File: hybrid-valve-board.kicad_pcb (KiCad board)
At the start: 2 copper layers, 68 x 79 mm, 45 parts, among them J1 XV Supply, J10 ARM, J2 MCU Supply, J3 XV In, J4 XV In, J5 XV In, J6 Continuity, J7 XV Out, J8 XV Out, J9 XV Out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

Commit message: Move arming LED closer to arming switch
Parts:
- moved D10 6.06 mm to (133.0, 84.0), turned to 0 degrees
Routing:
- net +3V3: track 33.4 -> 27.2 mm
- net Net-(D10-K): track 2.51 -> 7.66 mm
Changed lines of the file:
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@@
 		(tags "SMD DIP DIL PDIP SMDIP 2.54mm 9.53mm 375mil")
 		(property "Reference" "U2"
-			(at 0 -3.6 0)
+			(at 0 0 0)
 			(layer "F.SilkS")
 			(effects
@@
 		(tags "SMD DIP DIL PDIP SMDIP 2.54mm 9.53mm 375mil")
 		(property "Reference" "U3"
-			(at 0 -3.6 0)
+			(at 0 0 0)
 			(layer "F.SilkS")
 			(effects
@@
 		(tags "SMD DIP DIL PDIP SMDIP 2.54mm 9.53mm 375mil")
 		(property "Reference" "U4"
-			(at 0 -3.6 0)
+			(at 0 0 0)
 			(layer "F.SilkS")
 			(effects
@@
 	(footprint "LED_SMD:LED_0805_2012Metric_Pad1.15x1.40mm_HandSolder"
 		(layer "F.Cu")
-		(at 127.5 86.5 -90)
+		(at 133.025 84)
 		(descr "LED SMD 0805 (2012 Metric), square (rectangular) end terminal, IPC_7351 nominal, (Body size source: https://docs.google.com/spreadsheets/d/1BsfQQcO9C6DZCsRaXUlFlo91Tg2WpOkGARC1WS5S8t0/edit?usp=sharing), generated with kicad-footprint-generator")
 		(tags "LED handsolder")
 		(property "Reference" "D10"
-			(at 0 -2 90)
+			(at 3.475 0 360)
 			(layer "F.SilkS")
 			(effects
@@
 		)
 		(property "Value" "GREEN"
-			(at 0 1.65 90)
+			(at 0 1.65 360)
 			(layer "F.Fab")
 			(effects
@@
 		)
 		(property "Footprint" "LED_SMD:LED_0805_2012Metric_Pad1.15x1.40mm_HandSolder"
-			(at 0 0 -90)
+			(at 0 0 0)
 			(unlocked yes)
 			(layer "F.Fab")
@@
 		)
 		(property "Datasheet" "https://www.mouser.ca/datasheet/2/678/AV02_0551EN_DS_HSMx_Cxxx_25Mar2022-1827675.pdf"
-			(at 0 0 -90)
+			(at 0 0 0)
 			(unlocked yes)
 			(layer "F.Fab")
@@
 		)
 		(property "Description" "Light emitting diode"
-			(at 0 0 -90)
+			(at 0 0 0)
 			(unlocked yes)
 			(layer "F.Fab")
@@
 		)
 		(property "MPN" "HSMG-C170"
-			(at 0 0 -90)
+			(at 0 0 0)
 			(unlocked yes)
 			(layer "F.Fab")
@@
 		(attr smd)
 		(fp_line
-			(start -1.86 0.96)
-			(end 1 0.96)
+			(start -1.86 -0.96)
+			(end -1.86 0.96)
 			(stroke
 				(width 0.12)
@@
 		)
 		(fp_line
-			(start -1.86 -0.96)
-			(end -1.86 0.96)
+			(start -1.86 0.96)
+			(end 1 0.96)
 			(stroke
 				(width 0.12)
@@
 		)
 		(fp_line
-			(start -1.85 0.95)
-			(end -1.85 -0.95)
+			(start -1.85 -0.95)
+			(end 1.85 -0.95)
 			(stroke
 				(width 0.05)
@@
 		)
 		(fp_line
-			(start 1.85 0.95)
-			(end -1.85 0.95)
+			(start -1.85 0.95)
+			(end -1.85 -0.95)
 			(stroke
 				(width 0.05)
@@
 		)
 		(fp_line
-			(start -1.85 -0.95)
-			(end 1.85 -0.95)
+			(start 1.85 -0.95)
+			(end 1.85 0.95)
 			(stroke
 				(width 0.05)
@@
 		)
 		(fp_line
-			(start 1.85 -0.95)
-			(end 1.85 0.95)
+			(start 1.85 0.95)
+			(end -1.85 0.95)
 			(stroke
 				(width 0.05)
@@
 		)
 		(fp_line
-			(start -1 0.6)
-			(end 1 0.6)
+			(start -1 -0.3)
+			(end -1 0.6)
 			(stroke
 				(width 0.1)
@@
 		)
 		(fp_line
-			(start 1 0.6)
-			(end 1 -0.6)
+			(start -1 0.6)
+			(end 1 0.6)
 			(stroke
 				(width 0.1)
@@
 		)
 		(fp_line
-			(start -1 -0.3)
-			(end -1 0.6)
+			(start -0.7 -0.6)
+			(end -1 -0.3)
 			(stroke
 				(width 0.1)
@@
 		)
 		(fp_line
-			(start -0.7 -0.6)
-			(end -1 -0.3)
+			(start 1 -0.6)
+			(end -0.7 -0.6)
 			(stroke
 				(width 0.1)
@@
 		)
 		(fp_line
-			(start 1 -0.6)
-			(end -0.7 -0.6)
+			(start 1 0.6)
+			(end 1 -0.6)
 			(stroke
 				(width 0.1)
@@
 		)
 		(fp_text user "${REFERENCE}"
-			(at 0 0 90)
+			(at 0 0 360)
 			(layer "F.Fab")
 			(effects
@@
 		)
 		(pad "1" smd roundrect
-			(at -1.025 0 270)
+			(at -1.025 0)
 			(size 1.15 1.4)
 			(layers "F.Cu" "F.Paste" "F.Mask")
@@
 		)
 		(pad "2" smd roundrect
-			(at 1.025 0 270)
+			(at 1.025 0)
 			(size 1.15 1.4)
 			(layers "F.Cu" "F.Paste" "F.Mask")
@@
 	)
 	(segment
+		(start 134.05 78.51925)
+		(end 134.09925 78.47)
+		(width 0.8)
+		(layer "F.Cu")
+		(net 15)
+	)
+	(segment
 		(start 121.415 82.35425)
 		(end 125.29925 78.47)
@@
 	)
 	(segment
-		(start 134.09925 80.92575)
-		(end 134.09925 78.47)
-		(width 0.5)
+		(start 134.05 84)
+		(end 134.05 78.51925)
+		(width 0.8)
 		(layer "F.Cu")
 		(net 15)
@@
 	)
 	(segment
-		(start 127.5 87.525)
-		(end 134.09925 80.92575)
-		(width 0.5)
-		(layer "F.Cu")
-		(net 15)
-	)
-	(segment
 		(start 124.06075 93.81575)
 		(end 121.415 91.17)
@@
 	)
 	(segment
-		(start 127.5 85.475)
-		(end 125.025 85.475)
+		(start 127.5 84)
+		(end 132 84)
+		(width 0.5)
+		(layer "F.Cu")
+		(net 27)
+	)
+	(segment
+		(start 126 85.5)
+		(end 127.5 84)
+		(width 0.5)
+		(layer "F.Cu")
+		(net 27)
+	)
+	(segment
+		(start 125 85.5)
+		(end 126 85.5)
 		(width 0.5)
 		(layer "F.Cu")

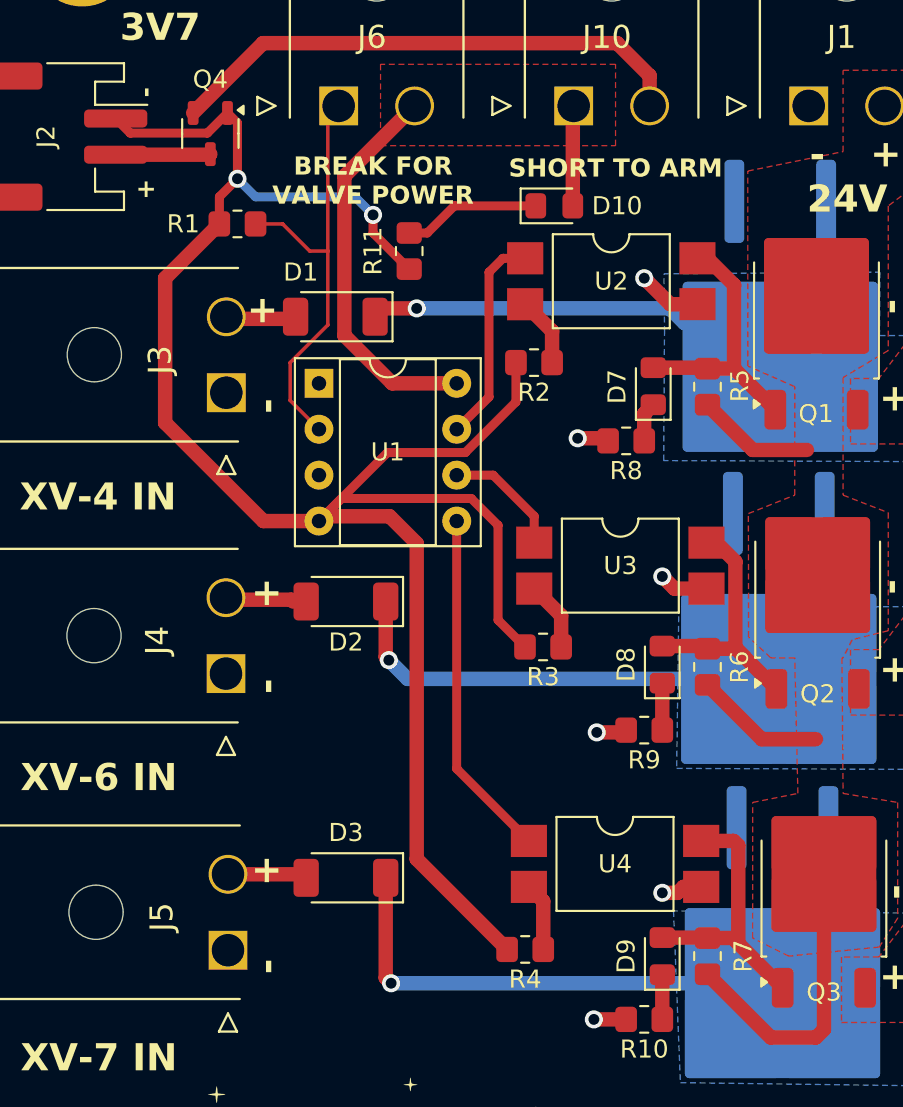
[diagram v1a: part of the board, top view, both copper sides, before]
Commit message: Added power decoupling capacitors for MCU
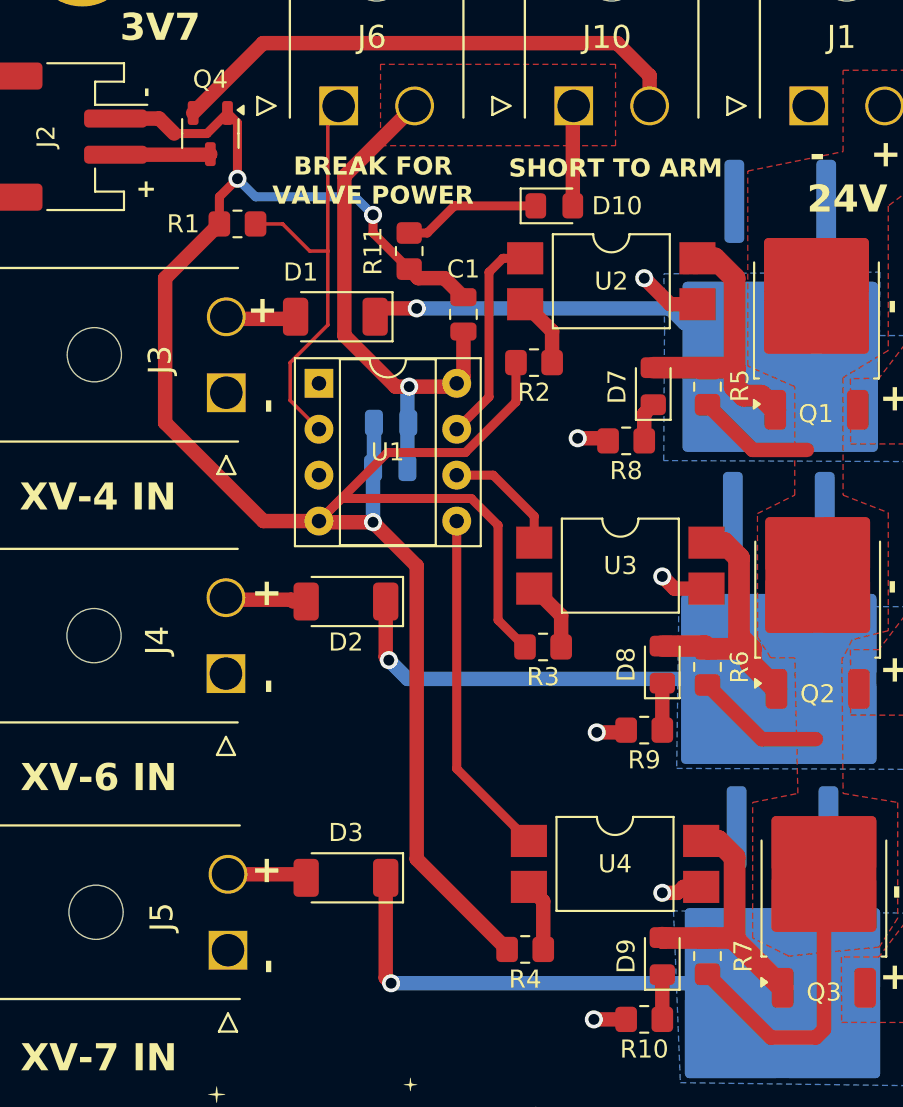
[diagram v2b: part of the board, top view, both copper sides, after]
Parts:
- added C1: 10u, Capacitor_SMD:C_0805_2012Metric, F.Cu at (128.0, 90.0)
- added C2: 100u, Capacitor_SMD:C_0805_2012Metric, B.Cu at (124.0, 96.0)
- added C3: 100u, Capacitor_SMD:C_0805_2012Metric, B.Cu at (124.0, 98.5)
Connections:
- net +3V3 renamed VSYS
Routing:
- net MCU_GND: track 113.8 -> 122.4 mm, vias 2 -> 3
- net VSYS: track 27.2 -> 34.9 mm, vias 0 -> 1
- net /XV7_ON_24V: track 15.4 -> 14.5 mm
- net /XV4_ON_24V: track 15.0 -> 15.8 mm

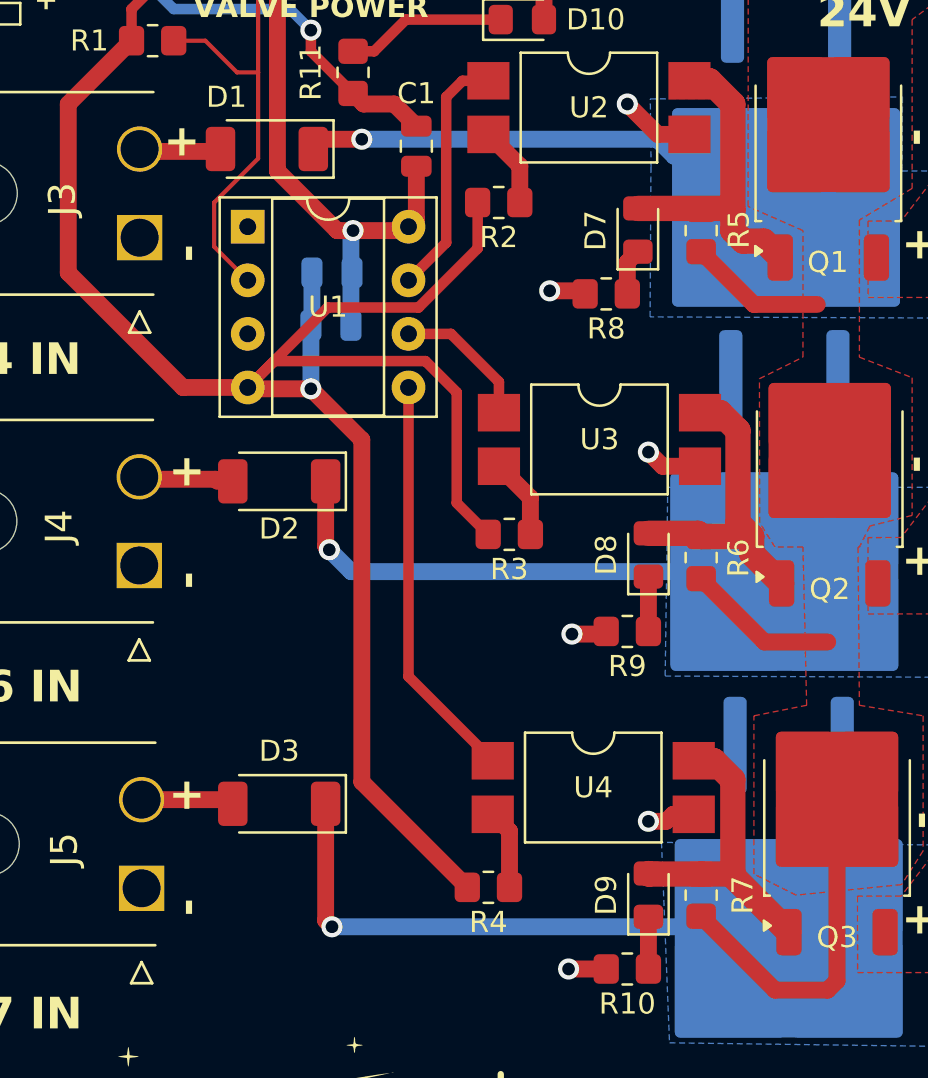
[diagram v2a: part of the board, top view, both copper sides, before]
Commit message: Thickened valve power traces from ground systems
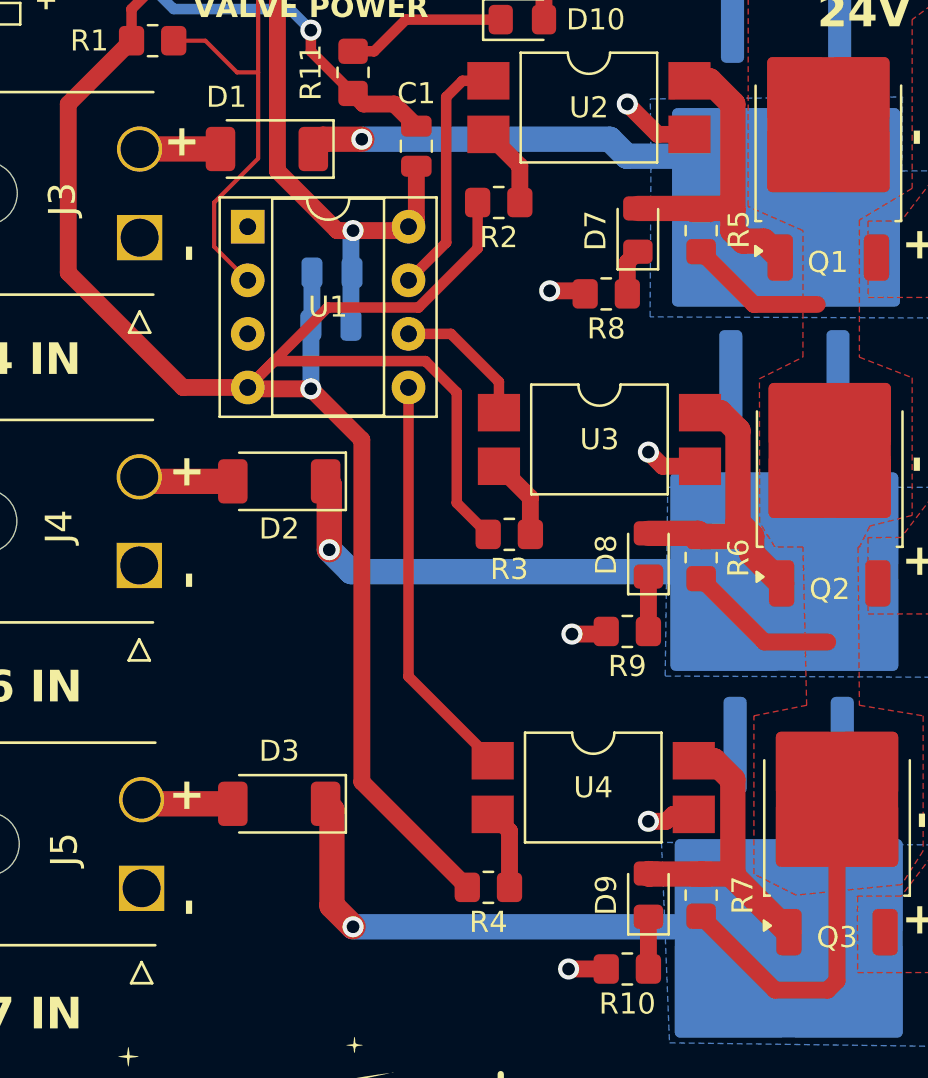
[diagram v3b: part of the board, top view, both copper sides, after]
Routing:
- net /XV7_PWR: track 25.6 -> 29.9 mm
- net Net-(D2-A): track 3.80 -> 4.68 mm
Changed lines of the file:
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@@
 		(start 125.415 89.67)
 		(end 123.577387 89.67)
-		(width 0.8)
+		(width 1.2)
 		(layer "F.Cu")
 		(net 1)
@@
 		(start 123.577387 89.67)
 		(end 123.115 90.132387)
-		(width 0.8)
+		(width 1.2)
 		(layer "F.Cu")
 		(net 1)
@@
 	)
 	(segment
-		(start 140.22 90.475)
+		(start 137.975 90.475)
 		(end 142.75 90.475)
-		(width 0.8)
+		(width 1.2)
+		(layer "B.Cu")
+		(net 1)
+	)
+	(segment
+		(start 137.17 89.67)
+		(end 137.975 90.475)
+		(width 1.2)
 		(layer "B.Cu")
 		(net 1)
@@
 	(segment
 		(start 125.415 89.67)
-		(end 139.415 89.67)
-		(width 0.8)
+		(end 137.17 89.67)
+		(width 1.2)
 		(layer "B.Cu")
 		(net 1)
-	)
-	(segment
-		(start 139.415 89.67)
-		(end 140.22 90.475)
-		(width 0.8)
-		(layer "B.Cu")
-		(net 1)
-	)
-	(segment
-		(start 118.59925 90.248137)
-		(end 118.715 90.132387)
-		(width 0.8)
-		(layer "F.Cu")
-		(net 2)
-	)
-	(segment
-		(start 114.996066 90.248137)
-		(end 118.59925 90.248137)
-		(width 0.8)
-		(layer "F.Cu")
-		(net 2)
 	)
 	(segment
@@
 	)
 	(segment
-		(start 123.8725 109.1275)
-		(end 123.7 108.955)
-		(width 0.8)
+		(start 118.715 90.132387)
+		(end 114.885874 90.132387)
+		(width 1.2)
+		(layer "F.Cu")
+		(net 2)
+	)
+	(segment
+		(start 114.885874 90.132387)
+		(end 114.883095 90.135166)
+		(width 1.2)
+		(layer "F.Cu")
+		(net 2)
+	)
+	(segment
+		(start 123.8725 106.05825)
+		(end 123.7 105.88575)
+		(width 1.2)
 		(layer "F.Cu")
 		(net 3)
 	)
 	(segment
-		(start 123.7 108.955)
-		(end 123.7 105.88575)
-		(width 0.8)
+		(start 123.8725 109.1275)
+		(end 123.8725 106.05825)
+		(width 1.2)
 		(layer "F.Cu")
 		(net 3)
@@
 	)
 	(segment
-		(start 124.91075 110.16575)
-		(end 145.445 110.16575)
-		(width 0.8)
+		(start 123.8725 109.1275)
+		(end 124.91075 110.16575)
+		(width 1.2)
 		(layer "B.Cu")
 		(net 3)
 	)
 	(segment
-		(start 123.8725 109.1275)
-		(end 124.91075 110.16575)
-		(width 0.8)
+		(start 124.91075 110.16575)
+		(end 145.445 110.16575)
+		(width 1.2)
 		(layer "B.Cu")
 		(net 3)
 	)
 	(segment
-		(start 118.478 105.78575)
-		(end 118.578 105.88575)
-		(width 0.8)
+		(start 119.3 105.88575)
+		(end 115.077772 105.88575)
+		(width 1.2)
 		(layer "F.Cu")
 		(net 4)
 	)
 	(segment
-		(start 114.977772 105.78575)
-		(end 118.478 105.78575)
-		(width 0.8)
+		(start 115.077772 105.88575)
+		(end 114.864801 105.672779)
+		(width 1.2)
 		(layer "F.Cu")
 		(net 4)
@@
 	)
 	(segment
+		(start 115.17331 121.17)
+		(end 114.976996 120.973686)
+		(width 1.2)
+		(layer "F.Cu")
+		(net 5)
+	)
+	(segment
+		(start 119.3 121.17)
+		(end 115.17331 121.17)
+		(width 1.2)
+		(layer "F.Cu")
+		(net 5)
+	)
+	(segment
 		(start 114.690195 121.086657)
 		(end 114.803166 120.973686)
@@
 	)
 	(segment
-		(start 114.803166 120.973686)
-		(end 119.103686 120.973686)
-		(width 0.8)
-		(layer "F.Cu")
-		(net 5)
-	)
-	(segment
-		(start 119.103686 120.973686)
-		(end 119.3 121.17)
-		(width 0.8)
-		(layer "F.Cu")
-		(net 5)
-	)
-	(segment
-		(start 123.7 126.7)
+		(start 124 121.47)
 		(end 123.7 121.17)
-		(width 0.8)
+		(width 1.2)
 		(layer "F.Cu")
 		(net 6)
 	)
 	(segment
-		(start 124 127)
-		(end 123.7 126.7)
-		(width 0.8)
+		(start 125 127)
+		(end 124 126)
+		(width 1.2)
+		(layer "F.Cu")
+		(net 6)
+	)
+	(segment
+		(start 124 126)
+		(end 124 121.47)
+		(width 1.2)
 		(layer "F.Cu")
 		(net 6)
 	)
 	(via
-		(at 124 127)
+		(at 125 127)
 		(size 1)
 		(drill 0.6)
 		(layers "F.Cu" "B.Cu")
+		(net 6)
+	)
+	(segment
+		(start 125 127)
+		(end 145.1 127)
+		(width 1.2)
+		(layer "B.Cu")
 		(net 6)
 	)
@@
 	)
 	(segment
-		(start 124 127)
-		(end 141 127)
-		(width 0.8)
+		(start 145.1 127)
+		(end 145.65 127.55)
+		(width 1.2)
 		(layer "B.Cu")
 		(net 6)

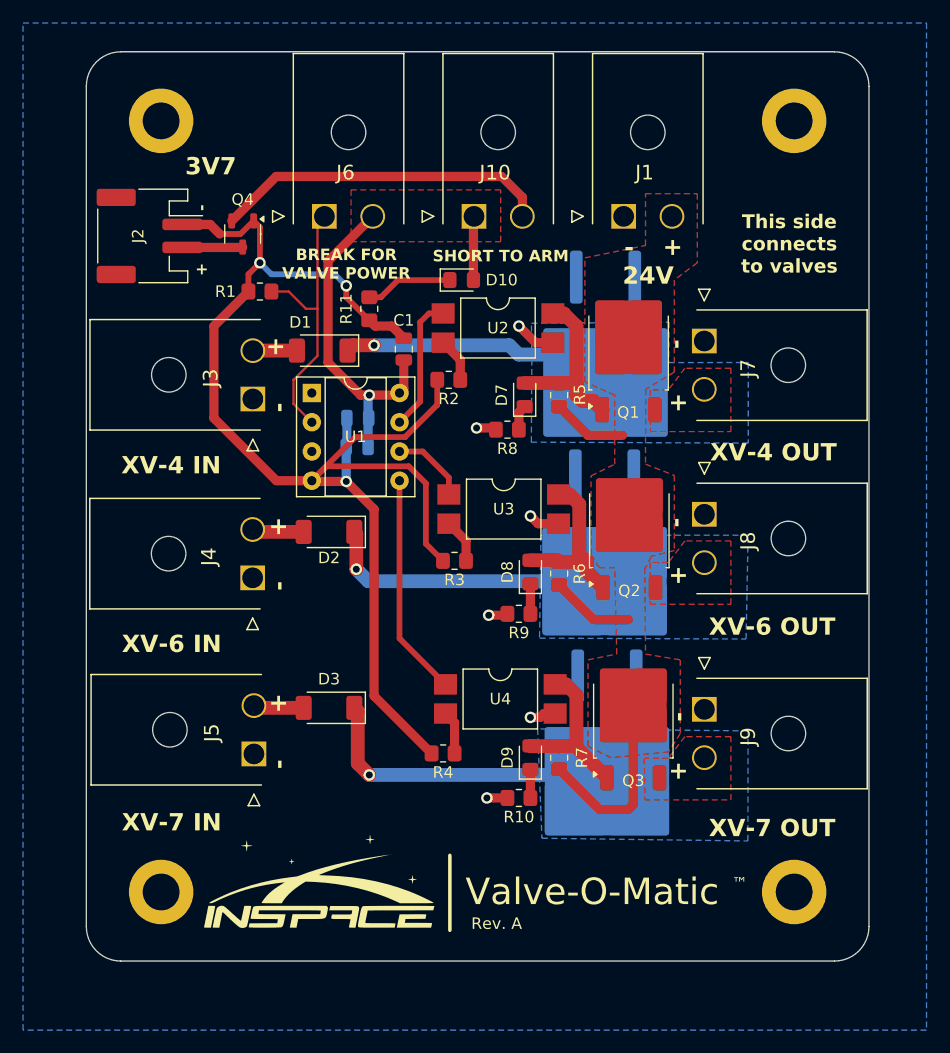
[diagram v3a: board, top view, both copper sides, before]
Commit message: Revision B, with correct connections for the PMOS switches :/
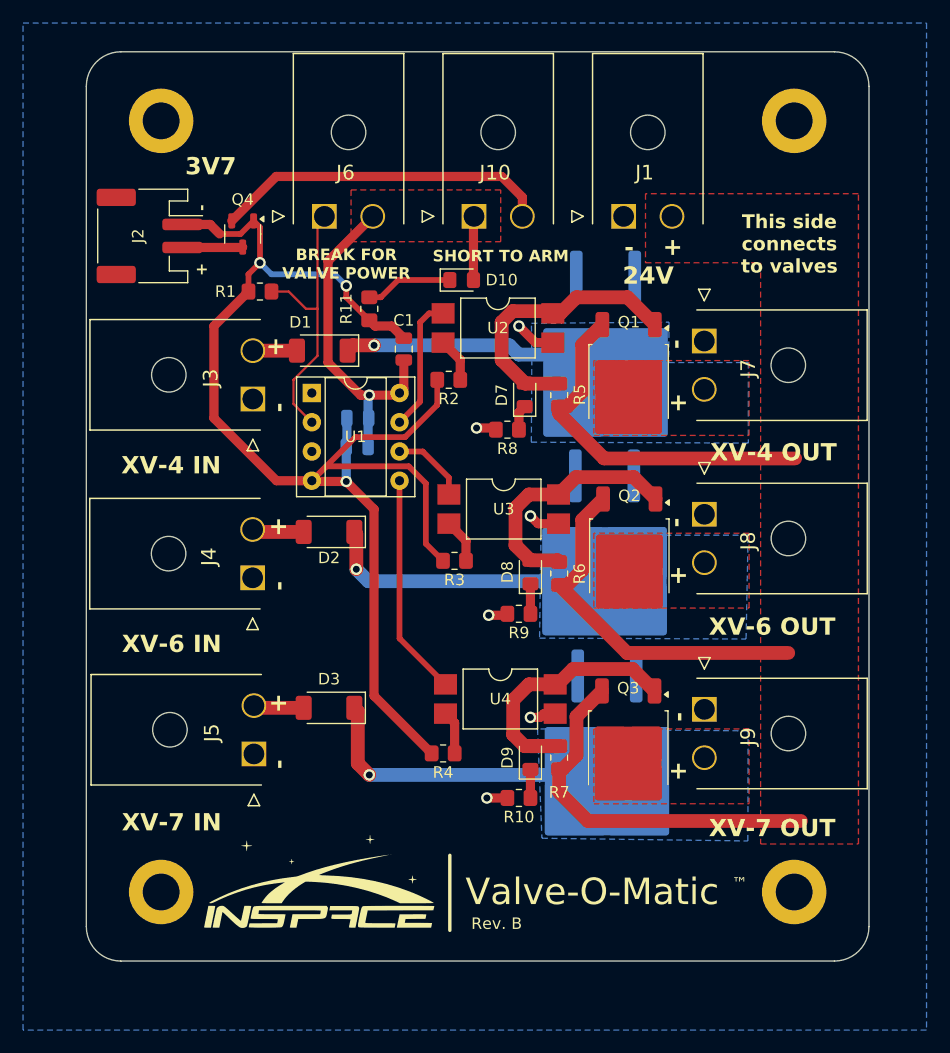
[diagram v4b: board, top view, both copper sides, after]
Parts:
- moved Q1 2.68 mm to (147.5, 92.9), turned to -90 degrees
- moved Q3 2.56 mm to (147.5, 124.7), turned to -90 degrees
- moved Q2 2.38 mm to (147.6, 108.1), turned to -90 degrees
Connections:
- Q1 pad 2: +24VBAT -> /XV4_PWR
- Q1 pad 3: /XV4_PWR -> +24VBAT
- Q2 pad 2: +24VBAT -> /XV6_PWR
- Q2 pad 3: /XV6_PWR -> +24VBAT
- Q3 pad 2: +24VBAT -> /XV7_PWR
- Q3 pad 3: /XV7_PWR -> +24VBAT
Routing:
- net +24VBAT: track 30.5 -> 96.2 mm
- net /XV7_ON_24V: track 14.5 -> 24.1 mm
- net /XV4_ON_24V: track 15.8 -> 24.5 mm
- net /XV6_ON_24V: track 15.2 -> 21.7 mm
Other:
- board text added: "Rev. B"
- board text removed: "Rev. A"
